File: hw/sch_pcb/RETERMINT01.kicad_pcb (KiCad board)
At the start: 2 copper layers, 61 parts, among them J1 Conn_02x05_Odd_Even, J10 RJ45_LED_Shielded, J11 HEADER_2x01_PARALLEL, J16 HEADER_2x01_PARALLEL, J3 MCX, J4 HEADER_2x01_PARALLEL, J5 HEADER_2x01_PARALLEL, J6 HEADER_2x05_PARALLEL, J7 Raspberry_Pi_4, J8 HEADER_2x01_PARALLEL, M1 HOLE, M2 HOLE, M3 HOLE, M4 HOLE, Q1 BC817-25, Q2 BC817-25, U1 USBLC6-2SC6, U2 MIC5504-3.3YM5, U3 NEO-M9N, U4 ADM2483xRW, U5 ADM2483xRW, U6 ADM2483xRW, U7 TPSM33606S5QRDNRQ1

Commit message: wip, layout
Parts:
- added C11: 1u, Capacitor_SMD:C_0805_2012Metric, F.Cu at (108.6, 151.4)
- added C12: 100n, Capacitor_SMD:C_0805_2012Metric, F.Cu at (108.7, 149.3)
- added C2: 1u, Capacitor_SMD:C_0805_2012Metric, F.Cu at (97.2, 128.6)
- added C3: 100n, Capacitor_SMD:C_0805_2012Metric, F.Cu at (93.8, 128.6)
- added C4: 1u, Capacitor_SMD:C_0805_2012Metric, F.Cu at (101.2, 127.5)
- added D8: SMCJ33A, Diode_SMD:D_SMC, F.Cu at (110.0, 136.4)
- added F1: 1A, Fuse:Fuse_0805_2012Metric, F.Cu at (76.3, 140.5)
- added F2: 1A, Fuse:Fuse_0805_2012Metric, F.Cu at (76.3, 136.4)
- added J2: Barrel_Jack_Switch, Connector_BarrelJack:BarrelJack_Horizontal, B.Cu at (73.1, 145.7)
- added JP2: SolderJumper_2_Open, Jumper:SolderJumper-2_P1.3mm_Open_RoundedPad1.0x1.5mm, F.Cu at (80.5, 59.3)
- added NT1: NetTie_2, NetTie:NetTie-2_SMD_Pad0.5mm, F.Cu at (72.6, 132.1)
- added R20: 220R, Resistor_SMD:R_0805_2012Metric, F.Cu at (132.6, 143.4)
- added R21: 220R, Resistor_SMD:R_0805_2012Metric, F.Cu at (135.1, 143.3)
- added TP1: GND_DIG, Connector_Pin:Pin_D1.4mm_L8.5mm_W2.8mm_FlatFork, F.Cu at (72.6, 135.6)
- added TP2: 24V, Connector_Pin:Pin_D1.4mm_L8.5mm_W2.8mm_FlatFork, F.Cu at (72.6, 139.5)
- added TP3: TestPoint, TestPoint:TestPoint_Pad_D1.5mm, F.Cu at (93.1, 120.2)
- added TP4: TestPoint, TestPoint:TestPoint_Pad_D1.5mm, F.Cu at (135.1, 137.0)
- C10: renamed from C7; footprint Mlab_R:SMD-0805 -> Capacitor_SMD:C_0805_2012Metric
- C5: renamed from C2; footprint Mlab_R:SMD-0805 -> Capacitor_SMD:C_0805_2012Metric
- C6: renamed from C5; footprint Mlab_R:SMD-0805 -> Capacitor_SMD:C_0805_2012Metric
- C7: renamed from C10; footprint Mlab_R:SMD-0805 -> Capacitor_SMD:C_0805_2012Metric
- C8: renamed from C3; footprint Mlab_R:SMD-0805 -> Capacitor_SMD:C_0805_2012Metric
- C9: renamed from C4; footprint Mlab_R:SMD-0805 -> Capacitor_SMD:C_0805_2012Metric
- D3, D6: footprint Mlab_D:LED_1206 -> LED_SMD:LED_1206_3216Metric
- J8: renamed from J3; value MCX -> u.fl
- R1: footprint Mlab_R:SMD-0805 -> Resistor_SMD:R_0805_2012Metric
- R10: renamed from R6; footprint Mlab_R:SMD-0805 -> Resistor_SMD:R_0805_2012Metric
- R11: renamed from R7; footprint Mlab_R:SMD-0805 -> Resistor_SMD:R_0805_2012Metric
- R12: renamed from R8; footprint Mlab_R:SMD-0805 -> Resistor_SMD:R_0805_2012Metric
- R13: renamed from R9; footprint Mlab_R:SMD-0805 -> Resistor_SMD:R_0805_2012Metric
- R14: renamed from R11; footprint Mlab_R:SMD-0805 -> Resistor_SMD:R_0805_2012Metric
- R15: renamed from R21; footprint Mlab_R:SMD-0805 -> Resistor_SMD:R_0805_2012Metric
- R16: renamed from R15; footprint Mlab_R:SMD-0805 -> Resistor_SMD:R_0805_2012Metric
- R17: renamed from R10; footprint Mlab_R:SMD-0805 -> Resistor_SMD:R_0805_2012Metric
- R18: renamed from R14; footprint Mlab_R:SMD-0805 -> Resistor_SMD:R_0805_2012Metric
- R19: renamed from R16; footprint Mlab_R:SMD-0805 -> Resistor_SMD:R_0805_2012Metric
- R2: renamed from R17; footprint Mlab_R:SMD-0805 -> Resistor_SMD:R_0805_2012Metric
- R3: renamed from R18; footprint Mlab_R:SMD-0805 -> Resistor_SMD:R_0805_2012Metric
- R4: renamed from R2; footprint Mlab_R:SMD-0805 -> Resistor_SMD:R_0805_2012Metric
- R5: renamed from R3; footprint Mlab_R:SMD-0805 -> Resistor_SMD:R_0805_2012Metric
- R6: renamed from R12; footprint Mlab_R:SMD-0805 -> Resistor_SMD:R_0805_2012Metric
- R7: renamed from R13; footprint Mlab_R:SMD-0805 -> Resistor_SMD:R_0805_2012Metric
- R8: renamed from R4; footprint Mlab_R:SMD-0805 -> Resistor_SMD:R_0805_2012Metric
- R9: renamed from R5; footprint Mlab_R:SMD-0805 -> Resistor_SMD:R_0805_2012Metric
- moved M3 157.3 mm to (143.2, 56.6)
- moved M4 132.8 mm to (70.4, 44.8)
- moved M2 117.4 mm to (143.4, 136.3)
- moved D6 87.1 mm to (83.2, 157.9)
- moved J10 37.9 mm to (67.8, 60.8)
- moved J11 36.4 mm to (124.8, 151.4)
- moved R7 36.1 mm to (107.9, 144.3)
- moved R6 35.8 mm to (108.7, 147.0), turned to 180 degrees
- moved D4 35.2 mm to (117.2, 136.6)
- moved D5 35.2 mm to (129.2, 136.7)
- moved J9 35.2 mm to (119.4, 113.4)
- moved JP3 35.2 mm to (122.7, 114.7)
- moved D7 35.2 mm to (121.0, 136.5)
- moved R15 35.2 mm to (108.5, 114.6)
- moved R16 35.2 mm to (134.1, 115.1)
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- renumbered D7 to D5, D5 to D7, J7 to J10, J10 to J11, J6 to J3, J11 to J6, J16 to J7, J8 to J9, JP2 to JP3, Q2 to Q1, Q1 to Q2, U7 to U1, U1 to U2, U2 to U3, U3 to U4, U4 to U5, U5 to U6, U6 to U7
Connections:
- C8 pad 1: Net-(D3-A) -> Net-(JP1-A)
- C9 pad 1: Net-(D3-A) -> Net-(JP1-A)
- D3 pad 2: Net-(D3-A) -> +3V3_GPS
- J11 pad 10: unconnected-(J10-Pad10) -> Net-(J11-Pad10)
- J11 pad 11: unconnected-(J10-Pad11) -> GND_OUT
- J11 pad 12: unconnected-(J10-Pad12) -> Net-(J11-Pad12)
- J11 pad 9: unconnected-(J10-Pad9) -> GND_OUT
- J11 pad SH: unconnected-(J10-PadSH) -> GND_OUT
- JP1 pad 1: Net-(D3-A) -> Net-(JP1-A)
- JP1 pad 3: unconnected-(JP1-B-Pad3) -> +3V3
- M1 pad 1: GND -> GND_DIG
- M2 pad 1: GND -> GND_DIG
- M3 pad 1: GND -> GND_DIG
- M4 pad 1: GND -> GND_DIG
- U3 pad 5: Net-(D3-A) -> Net-(JP1-A)
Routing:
- net +3V3_GPS: track 69.6 -> 176.7 mm, vias 2 -> 4
- net +3V3: track 0.00 -> 103.8 mm, vias 0 -> 4
- net /RX: track 0.00 -> 90.2 mm, vias 0 -> 1
- net Net-(D6-K): track 0.00 -> 84.8 mm, vias 0 -> 2
- net /TX: track 0.00 -> 74.3 mm, vias 0 -> 1
- net +24V_OUT: track 21.0 -> 72.7 mm, vias 0 -> 3
- net GNDPWR: track 0.00 -> 38.6 mm
- net /TIMEPULSE: track 26.0 -> 63.5 mm, vias 0 -> 1
- net /PWR_OFF: track 0.00 -> 30.9 mm
- net Net-(J11-Pad12): track 0.00 -> 23.6 mm, vias 0 -> 3
- net +5V_OUT: track 41.6 -> 64.4 mm
- net +24V_IN: track 0.00 -> 13.1 mm
- net Net-(JP1-A): track 0.00 -> 9.39 mm
- net Net-(J11-Pad10): track 0.00 -> 9.07 mm, vias 0 -> 1
- net Net-(PS1-+VIN_(VCC)): track 0.00 -> 8.87 mm
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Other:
- board outline added: 74 x 119.5 mm

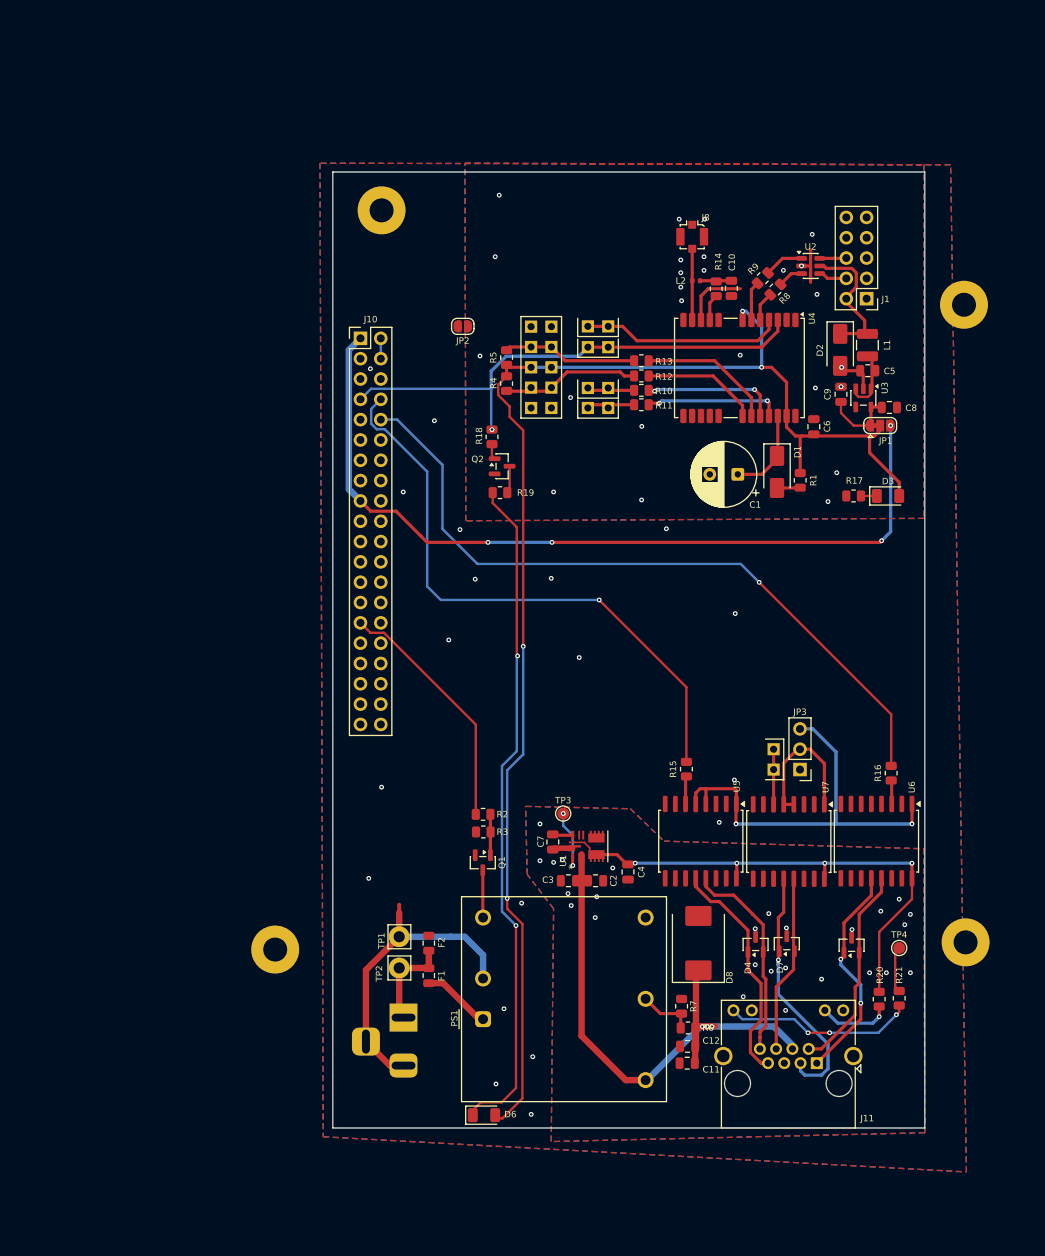
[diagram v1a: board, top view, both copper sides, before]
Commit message: PS1 default-off: add pull-up on Q1 base, rework R2/R3
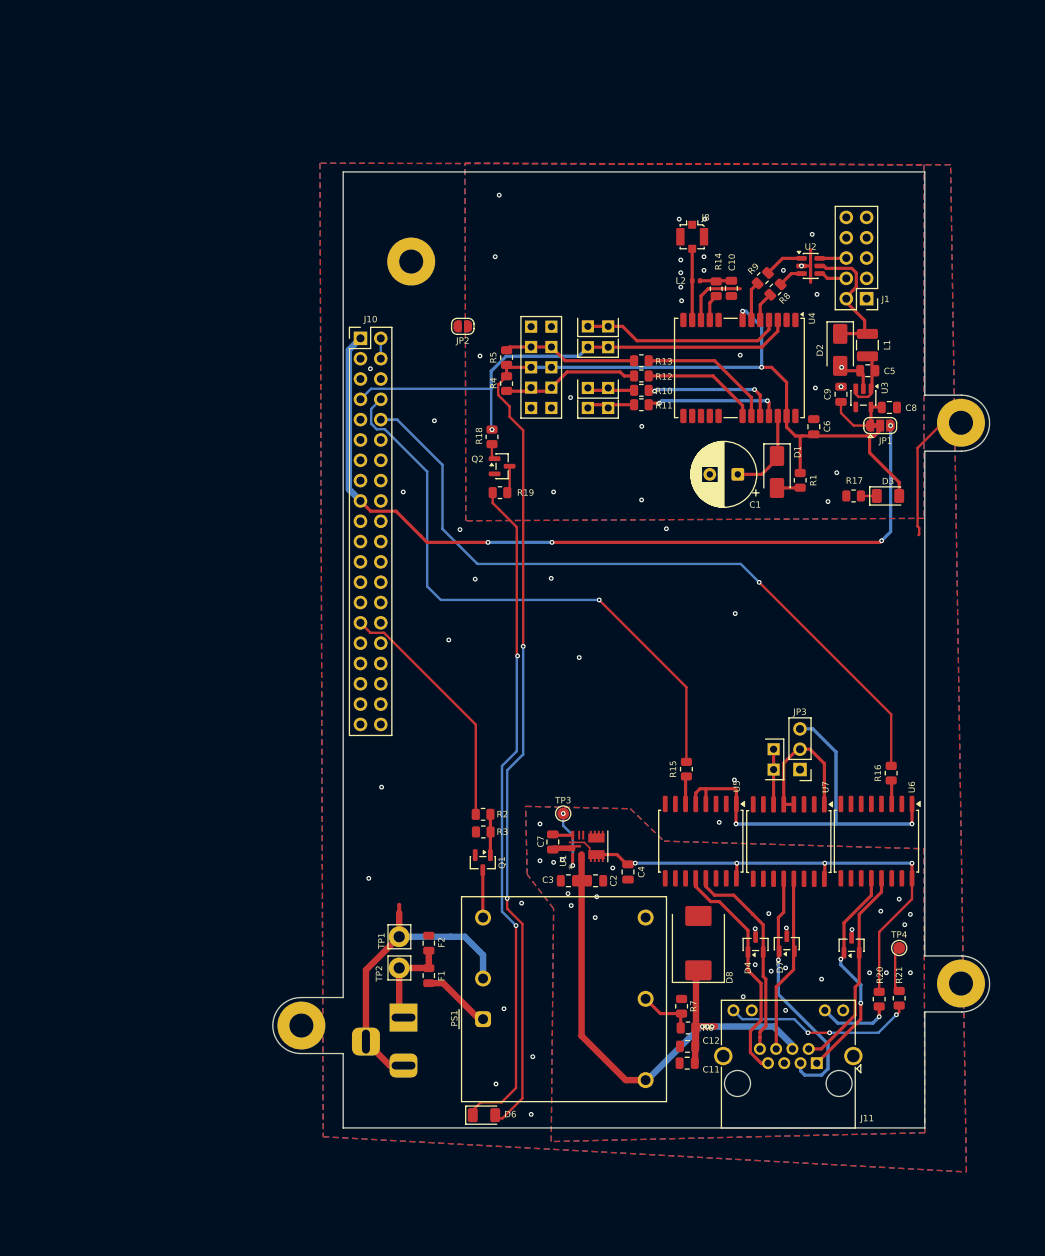
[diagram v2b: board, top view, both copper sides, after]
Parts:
- M4: moved to B.Cu
- moved M3 14.8 mm to (142.8, 71.3)
- moved M1 10.0 mm to (60.4, 146.7)
- moved M4 7.39 mm to (74.1, 51.2)
- moved M2 5.18 mm to (142.8, 141.4)
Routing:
- net GND_DIG: track 0.00 -> 17.8 mm
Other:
- board size 74 x 119.5 mm -> 89.6 x 119.5 mm

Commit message: update layout
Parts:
- added R20: 220R, Resistor_SMD:R_0805_2012Metric, F.Cu at (115.6, 132.9)
- added R21: 220R, Resistor_SMD:R_0805_2012Metric, F.Cu at (130.6, 132.0)
- added R23: 220R, Resistor_SMD:R_0805_2012Metric, F.Cu at (121.3, 131.2)
- added R3: 10k, Resistor_SMD:R_0805_2012Metric, F.Cu at (83.1, 118.2)
- R2: value 10k -> 1k
- R4: renamed from R3; value 100k -> 10k
- renumbered R9 to R10, R10 to R11, R11 to R12, R12 to R13, R13 to R14, R14 to R15, R15 to R16, R16 to R17, R17 to R18, R18 to R19, R19 to R22, R20 to R24, R21 to R25, R4 to R5, R5 to R6, R6 to R7, R7 to R8, R8 to R9
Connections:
- net Net-(PS1-COMMON) renamed /TRIM
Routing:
- net +3V3: track 103.8 -> 136.6 mm, vias 4 -> 6
- net Net-(Q1-B): track 5.10 -> 7.21 mm
- net /TX: track 74.3 -> 72.4 mm
- net /PWR_OFF: track 30.9 -> 32.1 mm

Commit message: update hader position
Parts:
- moved J10 15.3 mm to (67.7, 45.5)
- moved M4 11.0 mm to (83.2, 45.0)
- moved J11 0.75 mm to (124.0, 151.4)
- moved C8 0.23 mm to (134.1, 69.4)
- moved R6 0.21 mm to (86.0, 63.0)
- moved R12 0.20 mm to (102.9, 69.3)
- moved R14 0.15 mm to (102.9, 63.4)
- moved L1 0.14 mm to (131.1, 61.5)
- moved C10 0.12 mm to (114.2, 54.6)
- moved R13 0.10 mm to (102.9, 65.4)
- moved R11 0.06 mm to (102.9, 67.4)
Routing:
- net /TIMEPULSE: track 63.5 -> 81.4 mm, vias 1 -> 3
- net /RX: track 90.2 -> 104.3 mm, vias 1 -> 2
- net /TX: track 72.4 -> 86.3 mm, vias 1 -> 2
- net /PWR_OFF: track 32.1 -> 45.8 mm
- net +3V3: track 136.6 -> 148.8 mm
- net Net-(J11-Pad10): track 9.07 -> 9.82 mm
- net Net-(J11-Pad12): track 23.6 -> 24.3 mm
- net GND_GPS: vias 25 -> 24
- net GND_DIG: vias 19 -> 24

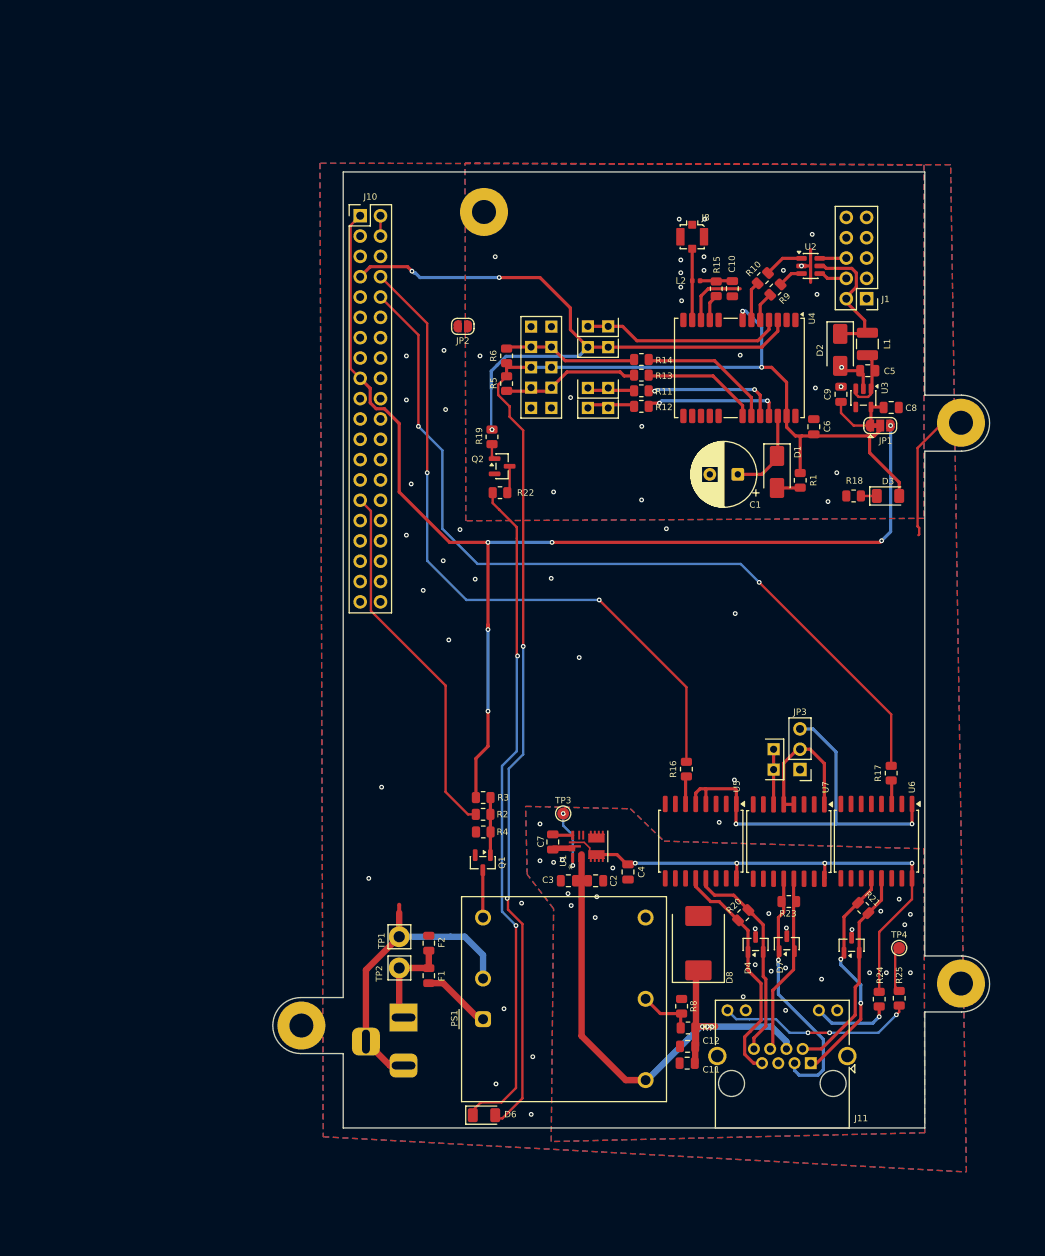
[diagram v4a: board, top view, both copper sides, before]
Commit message: Update DC/DC label
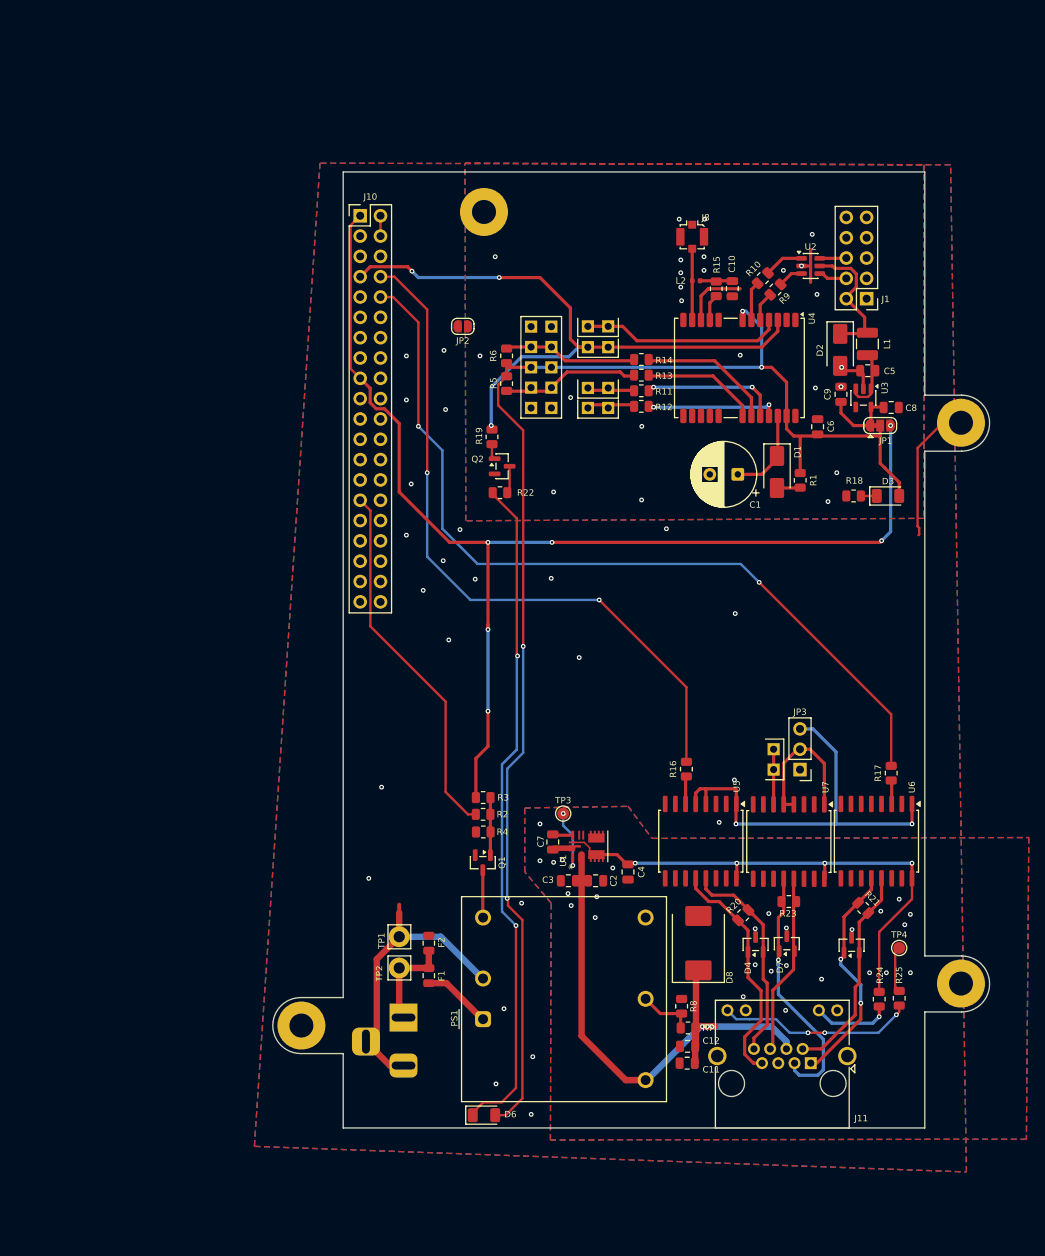
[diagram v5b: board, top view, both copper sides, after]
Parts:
- moved C6 0.47 mm to (124.9, 71.8)
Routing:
- net GNDPWR: track 38.6 -> 35.7 mm
- net /TIMEPULSE: track 81.4 -> 80.4 mm
- net /RX: track 104.3 -> 105.2 mm
- net /TX: track 86.3 -> 87.1 mm
- net Net-(U4-RXD/SPI_MOSI): track 17.0 -> 16.4 mm

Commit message: Fix #2 Fix DRC errors. Improve layout.
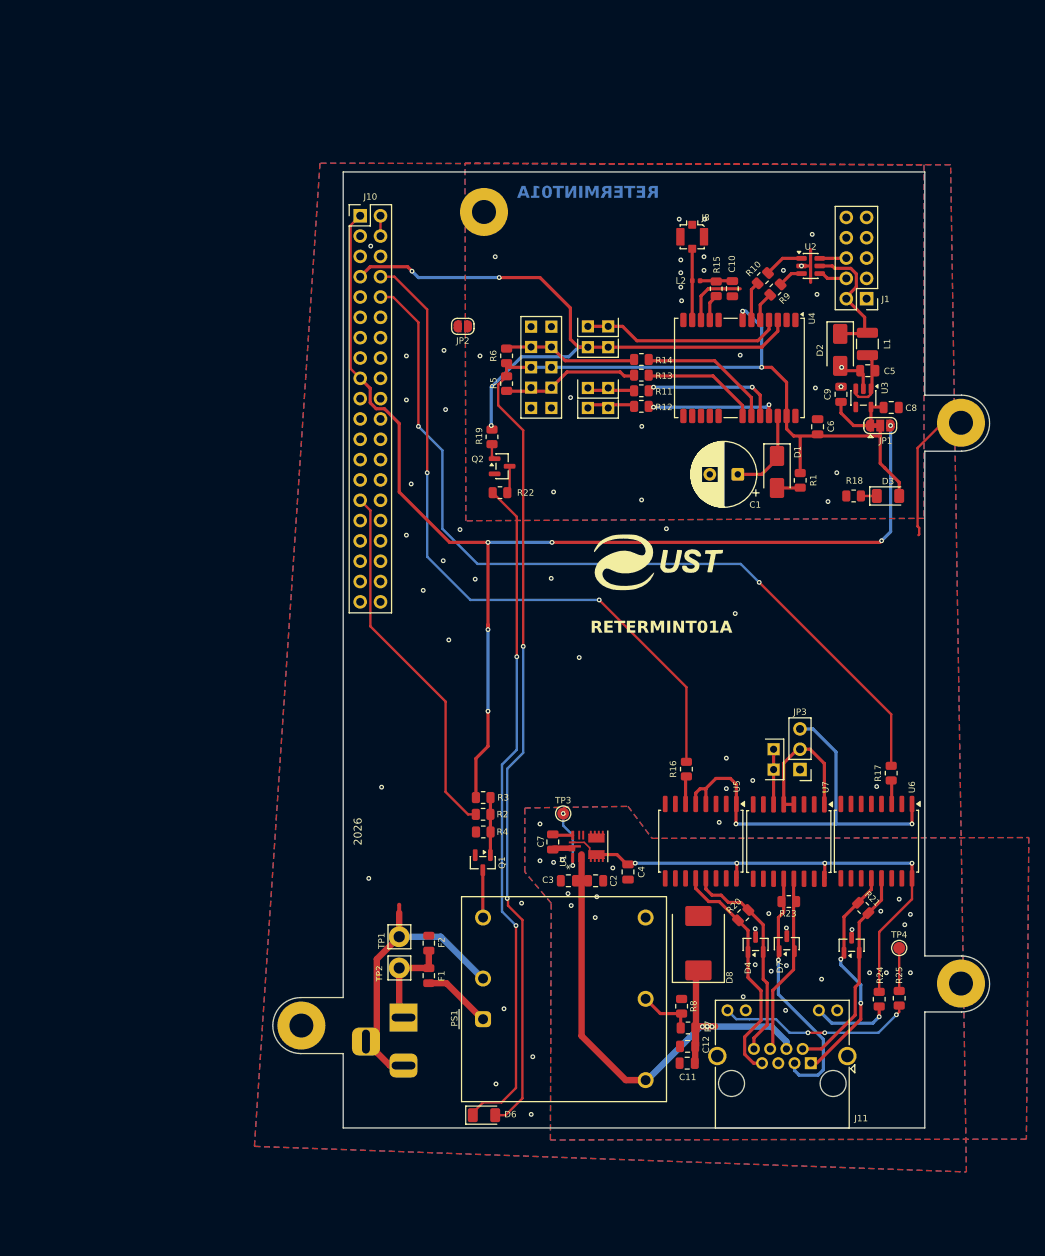
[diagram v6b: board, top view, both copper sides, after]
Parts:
- added G***: LOGO, MLAB_LOGA:UST, F.Cu at (105.0, 88.8)
- PS1: value THN_30-2423WI -> THN-30-2415WIR
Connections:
- net /PWR_OFF renamed /PWR_ON
- M1 pad 1: GND_DIG -> unconnected-(M1-Pad1)
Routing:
- net +3V3_DIG: track 52.1 -> 53.6 mm
- net GND_DIG: vias 24 -> 28
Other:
- board text added: "2026"
- board text added: "RETERMINT01A"
